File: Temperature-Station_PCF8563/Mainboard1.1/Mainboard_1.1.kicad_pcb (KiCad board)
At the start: 2 copper layers, 34 parts, among them J1 CONN_01X03, J2 CONN_01X15, J3 CONN_01X15, J4 SD_Card, J5 CONN_01X03, J6 CONN_01X02, J7 CONN_01X02, J8 CONN_01X02, J9 CONN_01X02, U1 LM1117-3.3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

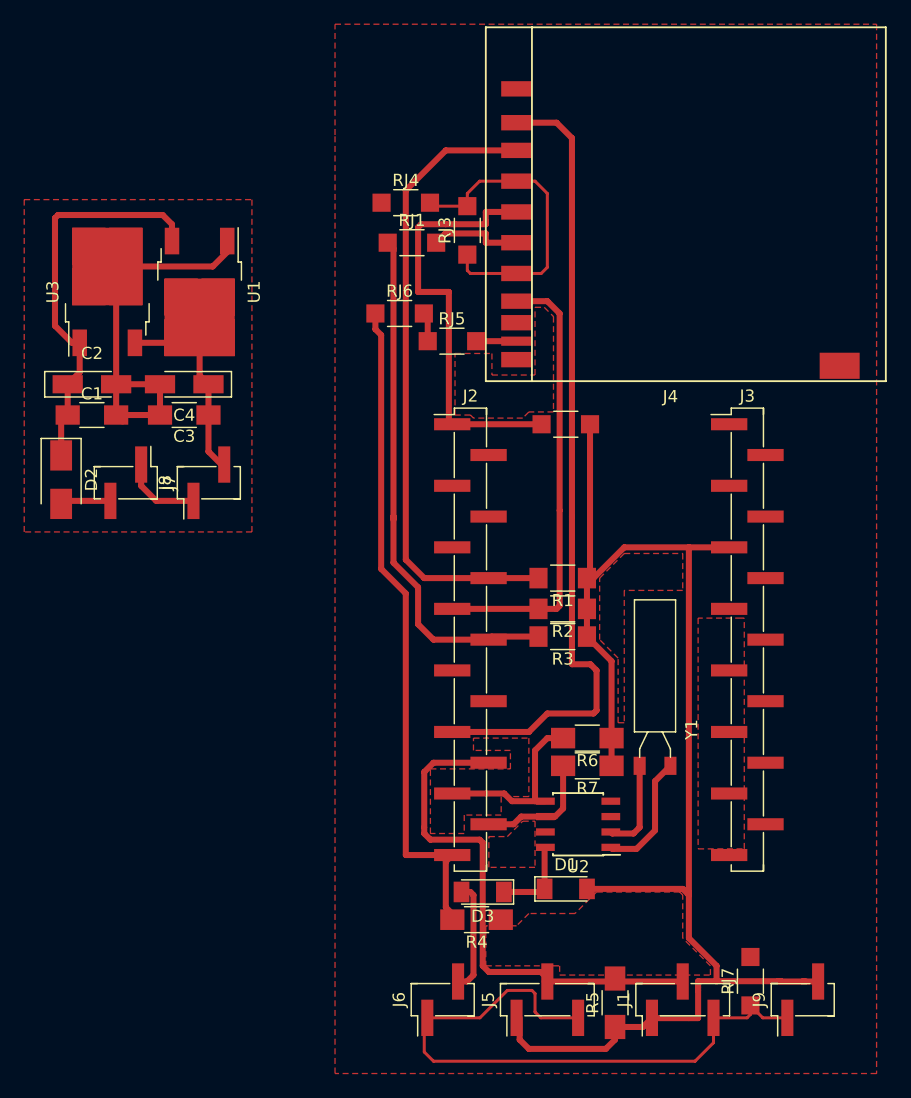
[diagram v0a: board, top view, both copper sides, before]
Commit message: Fixes
Added static/dhcp option for obtaining IP address
Little changes to code
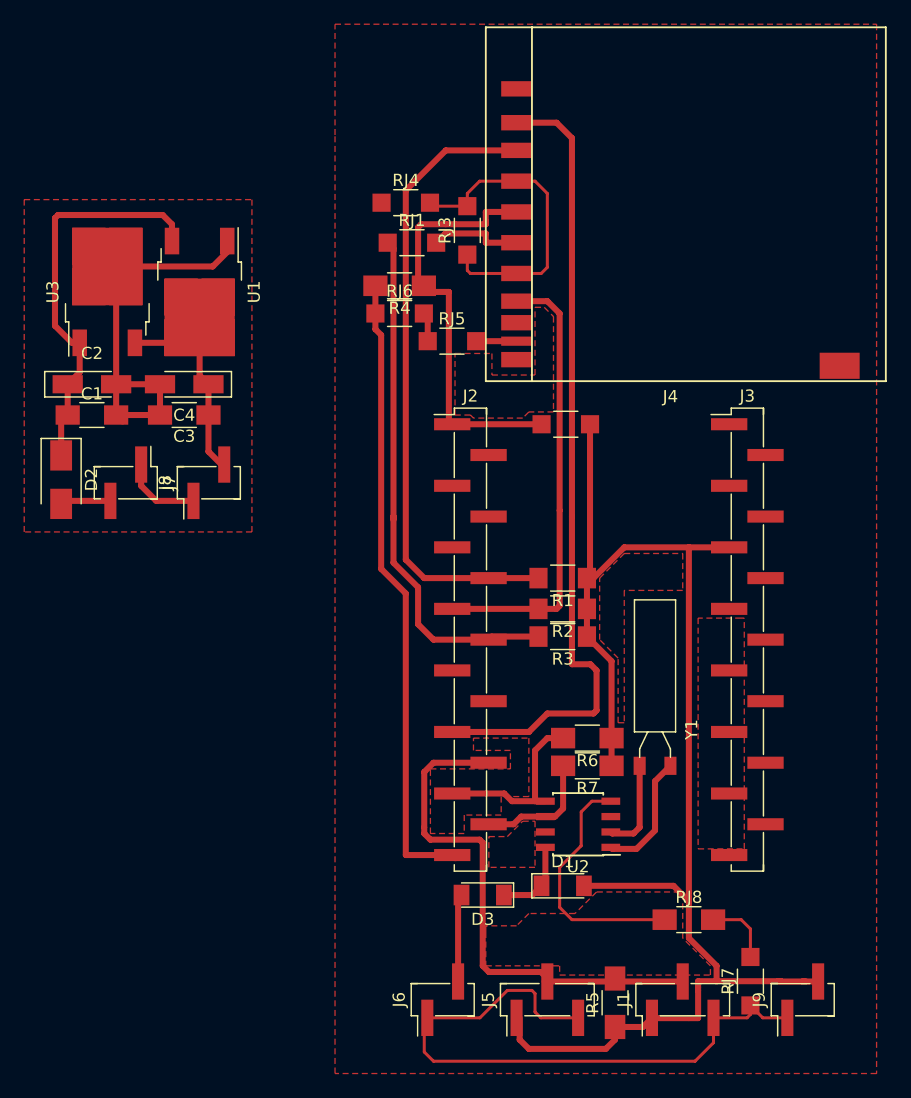
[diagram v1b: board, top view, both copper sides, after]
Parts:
- added RJ8: 0, Resistors_SMD:R_1206_HandSoldering, F.Cu at (155.2, 127.3)
- moved R4 52.7 mm to (131.3, 74.9)
- moved D1 0.36 mm to (144.8, 124.5)
- moved D3 0.25 mm to (138.2, 125.2)
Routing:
- net GND: track 79.4 -> 105.6 mm
- net SD_D: track 55.7 -> 52.5 mm
- net Net-(D3-Pad2): track 9.19 -> 7.25 mm
- net 3V3: track 158.4 -> 157.8 mm
